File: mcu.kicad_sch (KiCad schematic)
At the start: 18 parts, among them J1 USB_C_Receptacle, SW1 SW_Push, SW2 SW_Push, U3 ESP32-C6-MINI-1, U4 AMS1117-3.3

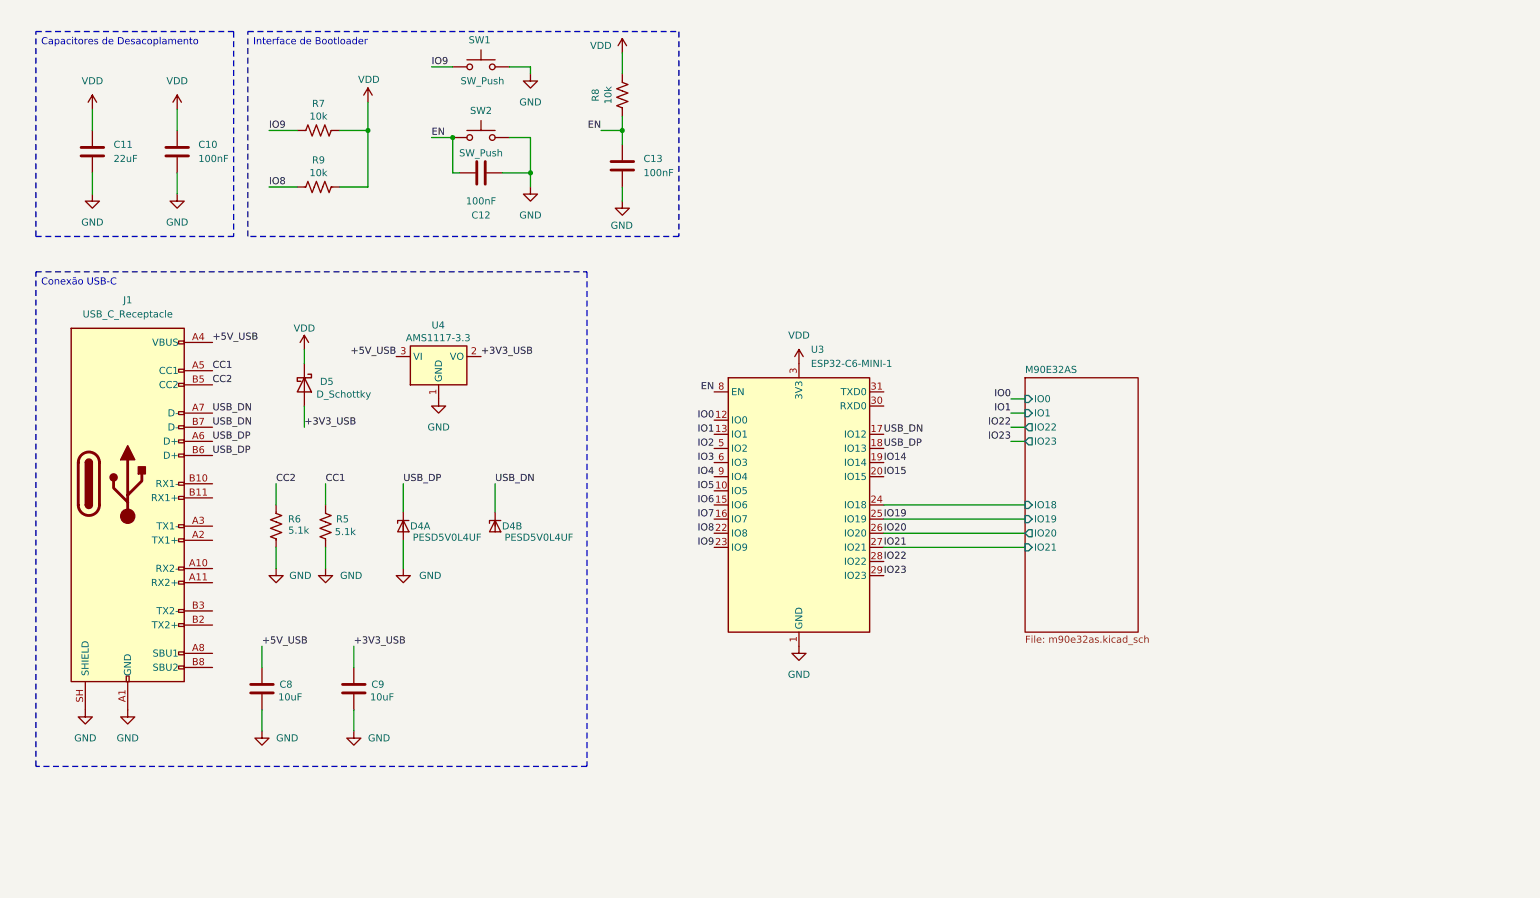
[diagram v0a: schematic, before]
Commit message: Checkpoint: MCU/M90E32AS/power_source rework, PCB layout, new sheets, library imports
- Rework mcu.kicad_sch, m90e32as.kicad_sch and power_source.kicad_sch: PM0/PM1/
  IRQ0/IRQ1 isolation wiring for the M90E32AS, USB-C native USB wiring, and
  related connector updates.
- Add analog_io.kicad_sch and digital_io.kicad_sch hierarchical sheets.
- Update ra5_2022.kicad_pcb layout and ra5_2022.kicad_pro settings.
- Import several LCSC components into the project library (connectors,
  inductor, SOT/SOIC footprints, USB-C connectors, power module).
- Fix import_lcsc_component.sh to normalize the "LCSC Part" field name to
  "LCSC Part #" on imported footprints too (previously only on symbols).
- Ignore local .claude/ state (worktrees/session data) in .gitignore.

Co-Authored-By: Claude Sonnet 5 <noreply@anthropic.com>
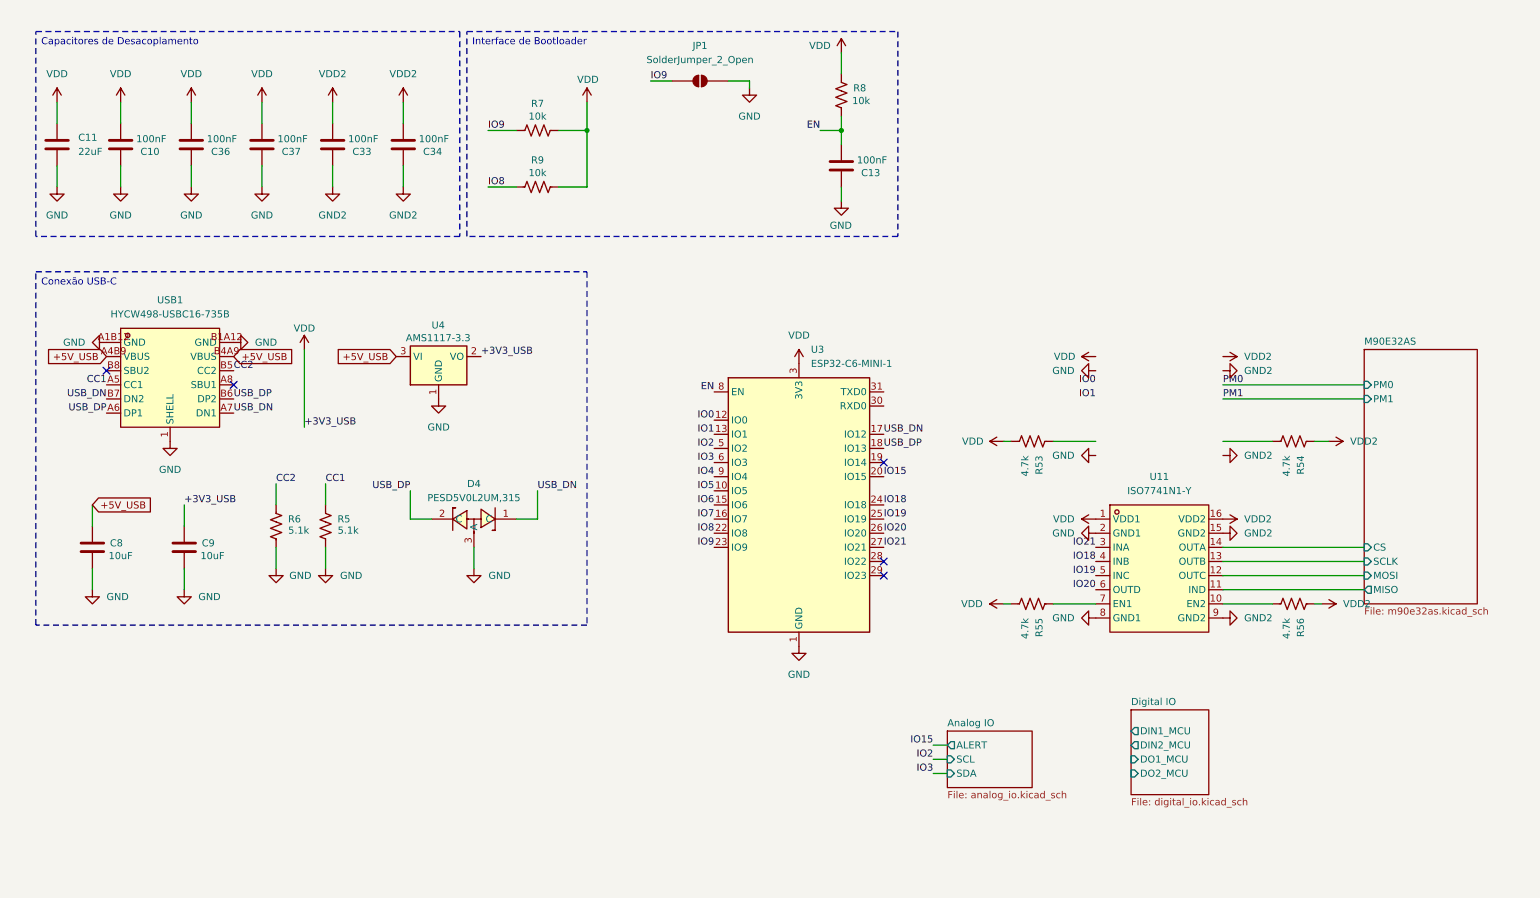
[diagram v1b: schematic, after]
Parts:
- removed C12: 100nF, Capacitor_SMD:C_0402_1005Metric, symbol Device:C
- removed D4: PESD5V0L4UF, Package_TO_SOT_SMD:SOT-886, symbol Power_Protection:PESD5V0L4UF
- removed D5: D_Schottky, Diode_SMD:D_SOD-123, symbol Device:D_Schottky
- removed J1: USB_C_Receptacle, Connector_USB:USB_C_Receptacle_GCT_USB4115-03-C, symbol Connector:USB_C_Receptacle
- removed SW1, SW2: SW_Push, Button_Switch_SMD:SW_SPST_TL3342, symbol Switch:SW_Push
- added C33, C34, C36, C37: 100nF, Capacitor_SMD:C_0201_0603Metric, symbol Device:C
- added D4: PESD5V0L2UM,315, ra5_2022:SOT-883-3_L1.0-W0.6-BR, symbol ra5_2022:PESD5V0L2UM,315
- added JP1: SolderJumper_2_Open, Jumper:SolderJumper-2_P1.3mm_Open_Pad1.0x1.5mm, symbol Jumper:SolderJumper_2_Open
- added R53, R54, R55, R56: 4.7k, Resistor_SMD:R_0402_1005Metric, symbol Device:R_US
- added U11: ISO7741N1-Y, ra5_2022:SOIC-16_L9.9-W3.9-P1.27-LS6.0-BL-1, symbol ra5_2022:ISO7741N1-Y
- added USB1: HYCW498-USBC16-735B, ra5_2022:USB-C-SMD_HYCW498-USBC16-735B, symbol ra5_2022:HYCW498-USBC16-735B
- C10, C13: footprint Capacitor_SMD:C_0402_1005Metric -> Capacitor_SMD:C_0201_0603Metric; LCSC Part # C22435941 -> C7393837; MPN CGA0402X7R104J250GT -> TCC0201X7R104K100ZT
- C11: footprint Capacitor_SMD:C_0402_1005Metric -> Capacitor_SMD:C_1210_3225Metric; LCSC Part # C6119784 -> C309062; MPN CGA0402X5R226M6R3GT -> CL32B226KAJNNNE
- R5, R6: LCSC Part # (none) -> C384321; MPN (none) -> WR04X512JTL
- U3: LCSC Part # (none) -> C5736265; MPN (none) -> ESP32-C6-MINI-1-N4
- U4: LCSC Part # (none) -> C50313802; MPN (none) -> AMS1117-3.3OF
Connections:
- net +3V3_USB is gone; now on net VDD: C9.2, U4.2 (VO)
- net +5V_USB: now also USB1.A4B9 (VBUS), USB1.B4A9 (VBUS)
- net CC1: now also USB1.A5 (CC1)
- net CC2: now also USB1.B5 (CC2)
- net EN: now also C13.2; no longer C13.1
- net GND: now also C10.1, C13.1, C36.1, C37.1, D4.3 (A), JP1.2 (B), U11.2 (GND1), U11.8 (GND1), USB1.1 (SHELL), USB1.A1B12 (GND), USB1.B1A12 (GND); no longer C10.2, C13.2
- net IO19: now also U11.5 (INC)
- net IO20: now also U11.6 (OUTD)
- net IO21: now also U11.3 (INA)
- net IO9: now also JP1.1 (A)
- net USB_DN: now also D4.1 (C), USB1.A7 (DN1), USB1.B7 (DN2)
- net USB_DP: now also D4.2 (C), USB1.A6 (DP1), USB1.B6 (DP2)
- net VDD: now also C10.2, C36.2, C37.2, R53.1, R55.1, U11.1 (VDD1); no longer C10.1
- net IO14: no longer names the net of U3.19 (IO14)
- net IO22: no longer names the net of U3.28 (IO22)
- net IO23: no longer names the net of U3.29 (IO23)
- net M90E32AS/IO18 renamed IO18
- net IO18: now also U11.4 (INB)
- new net: R55.2, U11.7 (EN1)
- new net: R56.1, U11.10 (EN2)
- new net GND2: C33.1, C34.1, U11.15 (GND2), U11.9 (GND2)
- new net M90E32AS/CS: U11.14 (OUTA)
- new net M90E32AS/MISO: U11.11 (IND)
- new net M90E32AS/MOSI: U11.12 (OUTC)
- new net M90E32AS/SCLK: U11.13 (OUTB)
- new net VDD2: C33.2, C34.2, R54.2, R56.2, U11.16 (VDD2)
- no-connect marks 0 -> 5
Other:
- added sheet Analog IO (analog_io.kicad_sch)
- added sheet Digital IO (digital_io.kicad_sch)
- sheet M90E32AS ports: added CS, MISO, MOSI, PM0, PM1, SCLK; removed IO0, IO1, IO18, IO19, IO20, IO21, IO22, IO23
- moved on the sheet: C8, C9, R7, R8, R9

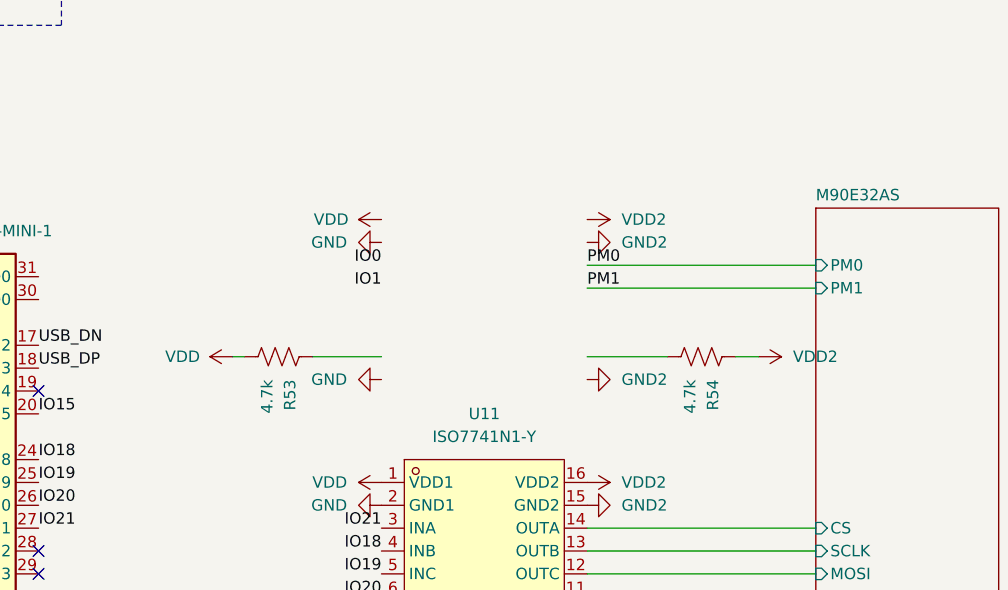
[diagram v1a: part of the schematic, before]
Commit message: Swap U7 isolator from ISO7742N1-Y to CS817X20LS
Only PM0/PM1 need to cross the M90E32AS isolation barrier now (IRQ0/IRQ1
dropped in favor of freeing GPIOs for the 4G modem RTS/CTS), so the
4-channel 2fwd/2rev isolator is replaced with the 2-channel, same-direction,
default-LOW CS817X20LS. Updates schematic, PCB footprint/routing and BOM.

Co-Authored-By: Claude Sonnet 5 <noreply@anthropic.com>
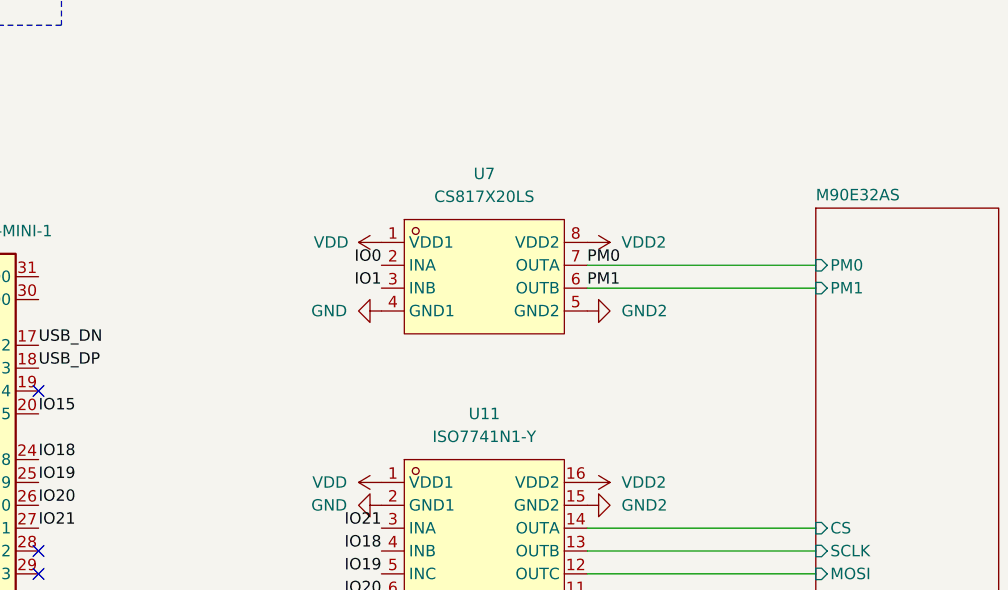
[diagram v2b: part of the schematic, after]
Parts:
- removed R53, R54: 4.7k, Resistor_SMD:R_0402_1005Metric, symbol Device:R_US
- added U7: CS817X20LS, ra5_2022:SOIC-8_L4.9-W3.9-P1.27-LS6.0-BL, symbol ra5_2022:CS817X20LS
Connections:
- net GND: now also U7.4 (GND1)
- net GND2: now also U7.5 (GND2)
- net IO0: now also U7.2 (INA)
- net IO1: now also U7.3 (INB)
- net PM0: now also U7.7 (OUTA)
- net PM1: now also U7.6 (OUTB)
- net VDD: now also U7.1 (VDD1)
- net VDD2: now also U7.8 (VDD2)

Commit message: Checkpoint: RA5 base board finished, M.2 shield interconnect defined
Base board (ra5_2022):
- Finalize component placement on ra5_2022.kicad_pcb; next step is routing
- Add STM8S003F3P to bridge the 2 digital inputs / 2 digital outputs onto
  the shared I2C bus (alongside the ADS1115), freeing up M.2 pins
- Wire J1 (M.2 Key-E) to a custom, non-spec-compliant 3.3V pinout: I2C
  (SDA/SCL/ALERT#) on the native pins, M90E32AS SPI reusing the SD/SDIO
  "SPI mode" pin convention (SCLK/MOSI/MISO/CS), PM0/PM1 on VENDOR_DEFINED
  pins, USB-C passthrough, full GND/VDD
- Fix AS0BC21-S40BE-7H footprint: pads 76/77 (shield/ground tabs, not part
  of the 75-pin M.2 spec) remapped onto the GND pin instead of dangling
- Swap the buck inductor (L2) for SLW5040S100MST (C182189): same 10uH,
  lower DCR, 5x5mm footprint to clear a routing constraint
- Remove the unused "Production" KiCad Design Variant and align the
  remaining "Develop" variant's footprints with the defaults -- a
  variant/default footprint mismatch was causing Update PCB from Schematic
  to silently duplicate footprints on every sync
- Clean up 10 further orphaned duplicate footprints left on the PCB from
  earlier design revisions (R11, R12, C14, C16, C17, C18, C29, C31, C32, C35)
- Fix 3D model paths across the shared library to use the RA5_2022_LIB
  environment variable instead of ${KIPRJMOD}, so previews resolve
  correctly from sibling projects too

New sibling project (ra5_shield_modem/):
- MCU + LTE modem card, built to the M.2 Key-E mechanical form factor to
  plug into the base board's J1
- Share the ra5_2022 parts library via sym-lib-table/fp-lib-table
- Add the timonsku/M.2-Card-Footprints submodule as a card-edge template

Co-Authored-By: Claude Sonnet 5 <noreply@anthropic.com>
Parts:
- removed C11: 22uF, Capacitor_SMD:C_1210_3225Metric, symbol Device:C
- removed C13, C33, C34, C36, C37: 100nF, Capacitor_SMD:C_0201_0603Metric, symbol Device:C
- removed JP1: SolderJumper_2_Open, Jumper:SolderJumper-2_P1.3mm_Open_Pad1.0x1.5mm, symbol Jumper:SolderJumper_2_Open
- removed R7, R8, R9: 10k, Resistor_SMD:R_0402_1005Metric, symbol Device:R_US
- removed U3: ESP32-C6-MINI-1, RF_Module:ESP32-C6-MINI-1, symbol RF_Module:ESP32-C6-MINI-1
- added C12, C14, C15, C16, C18: 100nF, Capacitor_SMD:C_0201_0603Metric, symbol Device:C
- added C17: 1uF, Capacitor_SMD:C_0402_1005Metric, symbol Device:C
- added H1: MountingScrew, MountingHole:MountingHole_2.2mm_M2_Pad_Via, symbol Auxiliary_Items:MountingScrew
- added J1: Bus_M.2_Socket_E, ra5_2022:CONN-SMD_AS0BC21-S48BE-7H, symbol Connector:Bus_M.2_Socket_E
- added J2: Conn_01x04_Socket, Connector_PinHeader_2.54mm:PinHeader_1x04_P2.54mm_Vertical, symbol Connector:Conn_01x04_Socket
- added R10, R11: 100R, Resistor_SMD:R_0402_1005Metric, symbol Device:R_US
- added U1: STM8S003F3P, Package_SO:TSSOP-20_4.4x6.5mm_P0.65mm, symbol MCU_ST_STM8:STM8S003F3P
- renumbered C8 to C11, C9 to C13, D4 to D3, R55 to R6, R6 to R7, R5 to R8, R56 to R9, U11 to U5, U7 to U6, U4 to U7
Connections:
- net IO0 is gone; now on net PM0: U6.2 (INA)
- net IO1 is gone; now on net PM1: U6.3 (INB)
- net Digital IO/DIN1_MCU: now also U1.13 (PC3)
- net Digital IO/DIN2_MCU: now also U1.14 (PC4)
- net Digital IO/DO1_MCU: now also U1.15 (PC5)
- net Digital IO/DO2_MCU: now also U1.16 (PC6)
- net GND: now also C12.1, C16.2, C17.2, C18.2, J1.1 (GND), J1.18 (GND), J1.33 (GND), J1.39 (GND), J1.45 (GND), J1.51 (GND), J1.57 (GND), J1.63 (GND), J1.69 (GND), J1.7 (GND), J1.75 (GND), J2.3 (Pin_3), U1.7 (VSS)
- net GND2: now also C14.1, C15.1
- net PM0: now also J1.38 (VENDOR_DEFINED); no longer U6.7 (OUTA)
- net PM1: now also J1.40 (VENDOR_DEFINED); no longer U6.6 (OUTB)
- net USB_DN: now also J1.5 (USB_D-)
- net USB_DP: now also J1.3 (USB_D+)
- net VDD: now also C12.2, C18.1, J1.2 (3.3V), J1.4 (3.3V), J1.72 (3.3V), J1.74 (3.3V), J2.4 (Pin_4), U1.9 (VDD)
- net VDD2: now also C14.2, C15.2
- net IO18 renamed SCLK
- net SCLK: now also J1.9 (SDIO_CLK)
- net IO19 renamed MOSI
- net MOSI: now also J1.11 (SDIO_CMD)
- net IO20 renamed MISO
- net MISO: now also J1.13 (SDIO_DATA0)
- net IO21 renamed CS
- net CS: now also J1.19 (SDIO_DATA3)
- new net: R11.2, U1.11 (PB5)
- new net: C17.1, U1.8 (VCAP)
- new net: R10.2, U1.12 (PB4)
- new net ALERT: J1.62 (~{ALERT}), U1.10 (PA3)
- new net M90E32AS/PM0: U6.7 (OUTA)
- new net M90E32AS/PM1: U6.6 (OUTB)
- new net NRST: C16.1, J2.1 (Pin_1), U1.4 (NRST)
- new net SCL: J1.60 (I2C_CLK), R10.1
- new net SDA: J1.58 (I2C_DATA), R11.1
- new net SWIM: J2.2 (Pin_2), U1.18 (PD1)
- no-connect marks 5 -> 51
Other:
- moved on the sheet: C11, C13, D3, R6, R7, R8, R9, U5, U6, U7, USB1
